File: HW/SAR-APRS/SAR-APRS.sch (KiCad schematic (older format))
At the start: 0 parts

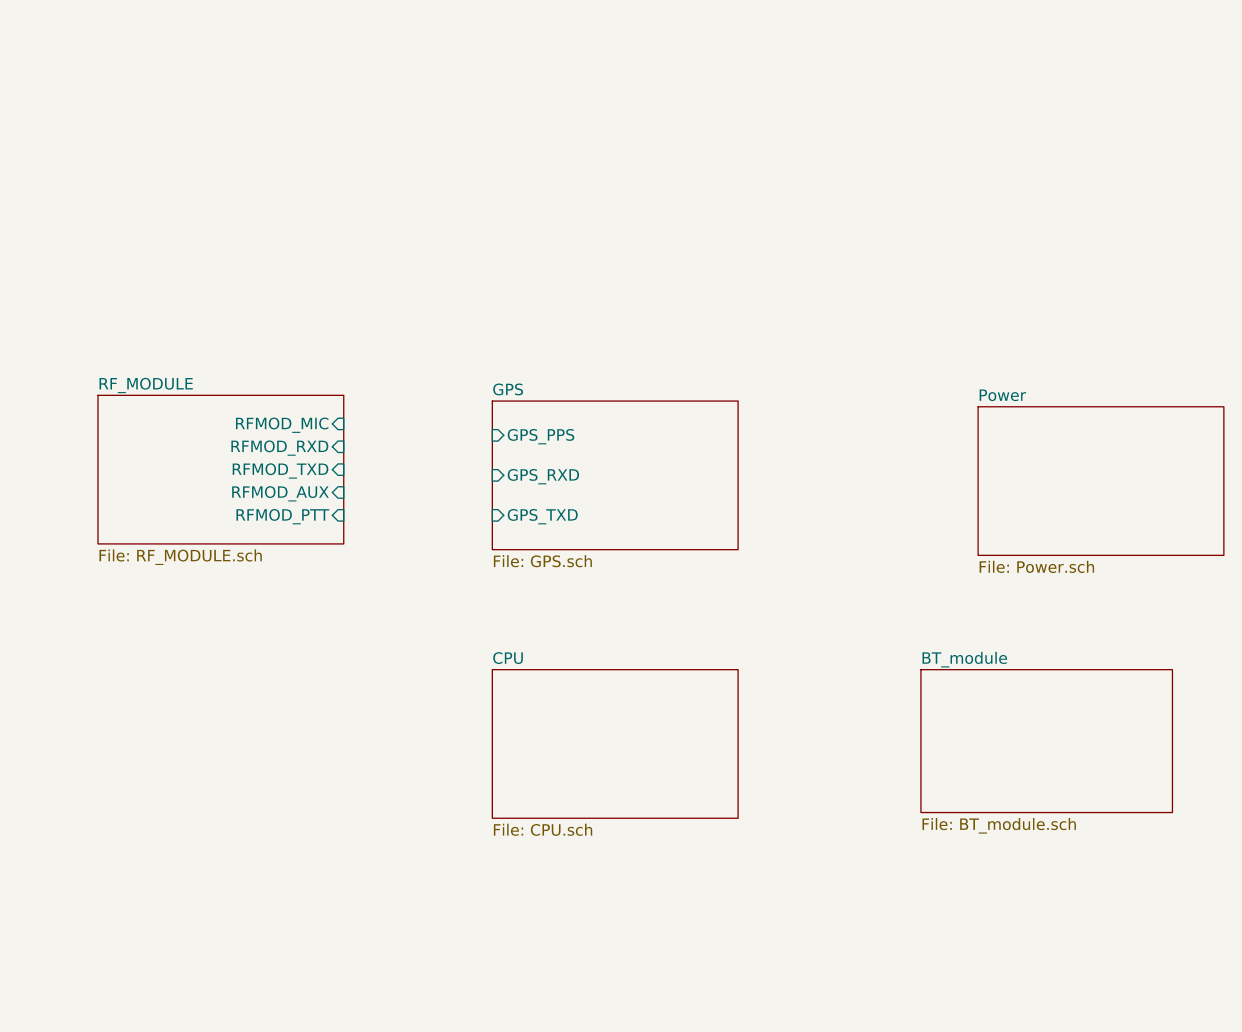
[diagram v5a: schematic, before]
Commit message: schematic update
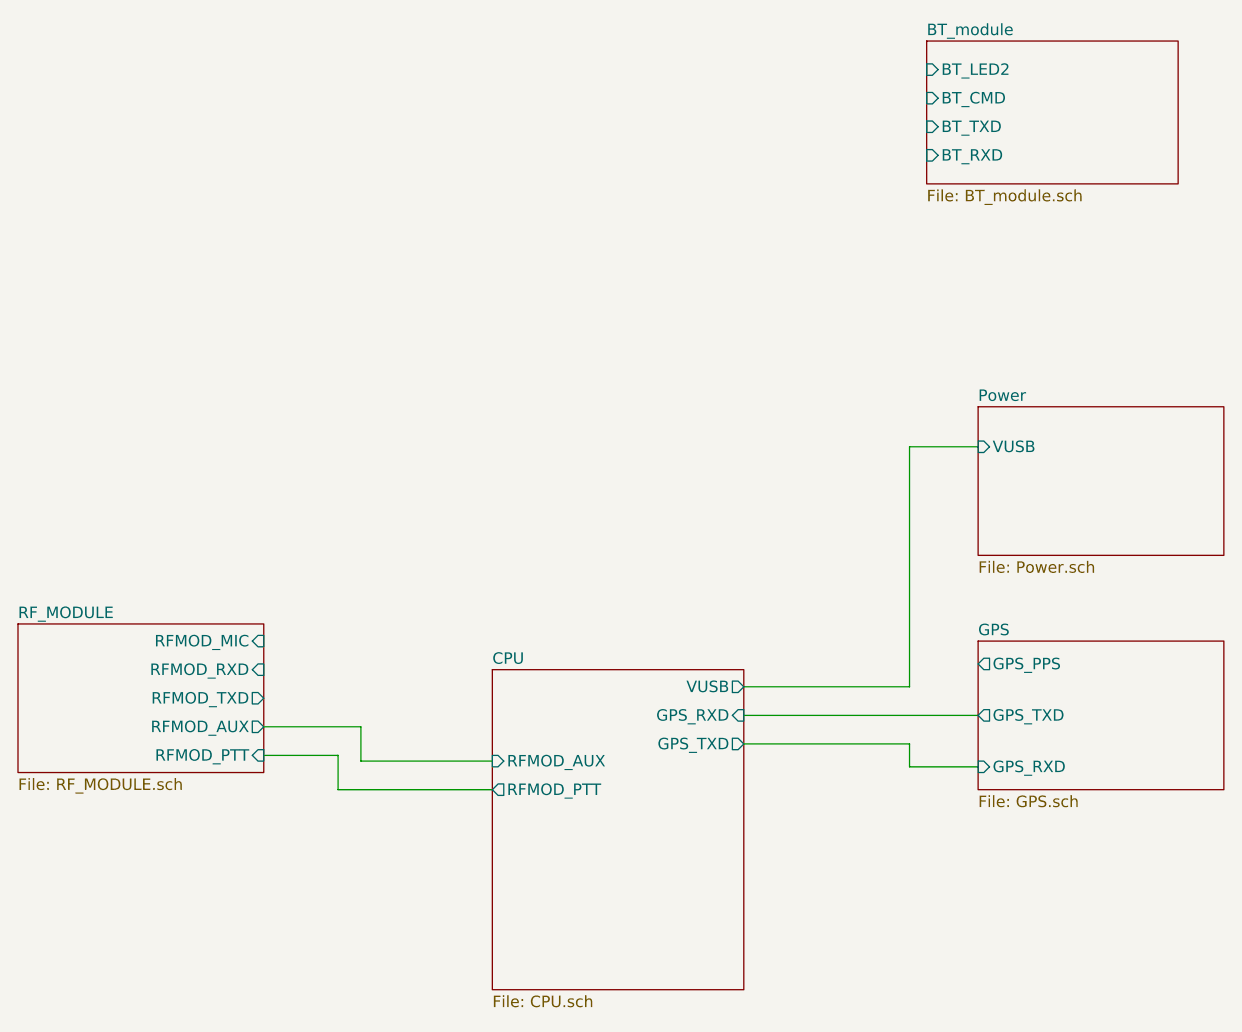
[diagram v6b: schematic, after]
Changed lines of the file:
@@
 $EndDescr
 $Sheet
-S 5700 4775 1075 650
+S 5350 5775 1075 650
 U 5C8B81A5
 F0 "RF_MODULE" 50
 F1 "RF_MODULE.sch" 50
-F2 "RFMOD_MIC" I R 6775 4900 50
-F3 "RFMOD_RXD" I R 6775 5000 50
-F4 "RFMOD_TXD" I R 6775 5100 50
-F5 "RFMOD_AUX" I R 6775 5200 50
-F6 "RFMOD_PTT" I R 6775 5300 50
+F2 "RFMOD_MIC" I R 6425 5850 50
+F3 "RFMOD_RXD" I R 6425 5975 50
+F4 "RFMOD_TXD" O R 6425 6100 50
+F5 "RFMOD_AUX" O R 6425 6225 50
+F6 "RFMOD_PTT" I R 6425 6350 50
 $EndSheet
 $Sheet
@@
 F0 "Power" 50
 F1 "Power.sch" 50
+F2 "VUSB" I L 9550 5000 50
 $EndSheet
 $Sheet
-S 7425 4800 1075 650
+S 7425 5975 1100 1400
+U 5CB07977
+F0 "CPU" 50
+F1 "CPU.sch" 50
+F2 "GPS_RXD" I R 8525 6175 50
+F3 "GPS_TXD" O R 8525 6300 50
+F4 "RFMOD_PTT" O L 7425 6500 50
+F5 "RFMOD_AUX" I L 7425 6375 50
+F6 "VUSB" O R 8525 6050 50
+$EndSheet
+$Sheet
+S 9325 3225 1100 625
+U 5C81D1BC
+F0 "BT_module" 50
+F1 "BT_module.sch" 50
+F2 "BT_LED2" I L 9325 3350 50
+F3 "BT_CMD" I L 9325 3475 50
+F4 "BT_TXD" I L 9325 3600 50
+F5 "BT_RXD" I L 9325 3725 50
+$EndSheet
+$Sheet
+S 9550 5850 1075 650
 U 5C97B601
 F0 "GPS" 50
 F1 "GPS.sch" 50
-F2 "GPS_PPS" I L 7425 4950 50
-F3 "GPS_RXD" I L 7425 5125 50
-F4 "GPS_TXD" I L 7425 5300 50
+F2 "GPS_PPS" O L 9550 5950 50
+F3 "GPS_TXD" O L 9550 6175 50
+F4 "GPS_RXD" I L 9550 6400 50
 $EndSheet
-$Sheet
-S 7425 5975 1075 650
-U 5CB07977
-F0 "CPU" 50
-F1 "CPU.sch" 50
-$EndSheet
-$Sheet
-S 9300 5975 1100 625
-U 5C81D1BC
-F0 "BT_module" 50
-F1 "BT_module.sch" 50
-$EndSheet
+Wire Wire Line
+	9550 6175 8525 6175
+Wire Wire Line
+	8525 6300 9250 6300
+Wire Wire Line
+	9250 6300 9250 6400
+Wire Wire Line
+	9250 6400 9550 6400
+Wire Wire Line
+	6425 6225 6850 6225
+Wire Wire Line
+	6850 6225 6850 6375
+Wire Wire Line
+	6850 6375 7425 6375
+Wire Wire Line
+	6425 6350 6750 6350
+Wire Wire Line
+	6750 6350 6750 6500
+Wire Wire Line
+	6750 6500 7425 6500
+Wire Wire Line
+	8525 6050 9250 6050
+Wire Wire Line
+	9250 6050 9250 5000
+Wire Wire Line
+	9250 5000 9550 5000
 $EndSCHEMATC

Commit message: schem and pcb update
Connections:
- wire segments 13 -> 14
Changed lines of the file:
@@
 EESchema Schematic File Version 4
 LIBS:SAR-APRS-cache
-EELAYER 28 0
+EELAYER 29 0
 EELAYER END
 $Descr A3 16535 11693
@@
 $EndDescr
 $Sheet
-S 5350 5775 1075 650
+S 5375 5000 1075 650
 U 5C8B81A5
 F0 "RF_MODULE" 50
 F1 "RF_MODULE.sch" 50
-F2 "RFMOD_MIC" I R 6425 5850 50
-F3 "RFMOD_RXD" I R 6425 5975 50
-F4 "RFMOD_TXD" O R 6425 6100 50
-F5 "RFMOD_AUX" O R 6425 6225 50
-F6 "RFMOD_PTT" I R 6425 6350 50
+F2 "RFMOD_MIC" I R 6450 5075 50
+F3 "RFMOD_RXD" I R 6450 5200 50
+F4 "RFMOD_TXD" O R 6450 5325 50
+F5 "RFMOD_AUX" O R 6450 5450 50
+F6 "RFMOD_PTT" I R 6450 5575 50
 $EndSheet
 $Sheet
-S 9550 4825 1075 650
+S 9650 3900 1075 650
 U 5C948828
 F0 "Power" 50
 F1 "Power.sch" 50
-F2 "VUSB" I L 9550 5000 50
+F2 "VUSB" I L 9650 4075 50
 $EndSheet
 $Sheet
-S 7425 5975 1100 1400
+S 7550 4950 1100 1625
 U 5CB07977
 F0 "CPU" 50
 F1 "CPU.sch" 50
-F2 "GPS_RXD" I R 8525 6175 50
-F3 "GPS_TXD" O R 8525 6300 50
-F4 "RFMOD_PTT" O L 7425 6500 50
-F5 "RFMOD_AUX" I L 7425 6375 50
-F6 "VUSB" O R 8525 6050 50
+F2 "GPS_RXD" I R 8650 5350 50
+F3 "GPS_TXD" O R 8650 5475 50
+F4 "RFMOD_PTT" O L 7550 5575 50
+F5 "RFMOD_AUX" I L 7550 5450 50
+F6 "VUSB" O R 8650 5025 50
+F7 "RFMOD_TXD" O L 7550 5200 50
+F8 "RFMOD_RXD" I L 7550 5325 50
+F9 "RFMOD_MIC" O L 7550 5075 50
+F10 "GPS_PPS" I R 8650 5200 50
+F11 "BT_TXD" O R 8650 6300 50
+F12 "BT_RXD" I R 8650 6425 50
+F13 "BT_LED2" O R 8650 6050 50
+F14 "BT_CMD" O R 8650 6175 50
 $EndSheet
 $Sheet
-S 9325 3225 1100 625
+S 9650 5925 1100 625
 U 5C81D1BC
 F0 "BT_module" 50
 F1 "BT_module.sch" 50
-F2 "BT_LED2" I L 9325 3350 50
-F3 "BT_CMD" I L 9325 3475 50
-F4 "BT_TXD" I L 9325 3600 50
-F5 "BT_RXD" I L 9325 3725 50
+F2 "BT_LED2" I L 9650 6050 50
+F3 "BT_CMD" I L 9650 6175 50
+F4 "BT_TXD" I L 9650 6300 50
+F5 "BT_RXD" I L 9650 6425 50
 $EndSheet
 $Sheet
-S 9550 5850 1075 650
+S 9650 4925 1075 650
 U 5C97B601
 F0 "GPS" 50
 F1 "GPS.sch" 50
-F2 "GPS_PPS" O L 9550 5950 50
-F3 "GPS_TXD" O L 9550 6175 50
-F4 "GPS_RXD" I L 9550 6400 50
+F2 "GPS_PPS" O L 9650 5200 50
+F3 "GPS_TXD" O L 9650 5350 50
+F4 "GPS_RXD" I L 9650 5475 50
 $EndSheet
 Wire Wire Line
-	9550 6175 8525 6175
+	9650 5350 8650 5350
 Wire Wire Line
-	8525 6300 9250 6300
+	8650 5025 9350 5025
 Wire Wire Line
-	9250 6300 9250 6400
+	9350 5025 9350 4075
 Wire Wire Line
-	9250 6400 9550 6400
+	9350 4075 9650 4075
 Wire Wire Line
-	6425 6225 6850 6225
+	6450 5575 7550 5575
 Wire Wire Line
-	6850 6225 6850 6375
+	6450 5450 7550 5450
 Wire Wire Line
-	6850 6375 7425 6375
+	6450 5325 7550 5325
 Wire Wire Line
-	6425 6350 6750 6350
+	6450 5200 7550 5200
 Wire Wire Line
-	6750 6350 6750 6500
+	7550 5075 6450 5075
 Wire Wire Line
-	6750 6500 7425 6500
+	8650 5475 9650 5475
 Wire Wire Line
-	8525 6050 9250 6050
+	8650 6425 9650 6425
 Wire Wire Line
-	9250 6050 9250 5000
+	8650 6300 9650 6300
 Wire Wire Line
-	9250 5000 9550 5000
+	8650 6175 9650 6175
+Wire Wire Line
+	8675 6050 9650 6050
 $EndSCHEMATC

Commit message: PCB update
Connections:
- wire segments 14 -> 15
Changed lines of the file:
@@
 F1 "RF_MODULE.sch" 50
 F2 "RFMOD_MIC" I R 6450 5075 50
-F3 "RFMOD_RXD" I R 6450 5200 50
-F4 "RFMOD_TXD" O R 6450 5325 50
+F3 "RFMOD_RXD" I R 6450 5325 50
+F4 "RFMOD_TXD" O R 6450 5200 50
 F5 "RFMOD_AUX" O R 6450 5450 50
 F6 "RFMOD_PTT" I R 6450 5575 50
@@
 	6450 5450 7550 5450
 Wire Wire Line
-	6450 5325 7550 5325
-Wire Wire Line
-	6450 5200 7550 5200
-Wire Wire Line
 	7550 5075 6450 5075
 Wire Wire Line
@@
 	8650 6175 9650 6175
 Wire Wire Line
-	8675 6050 9650 6050
+	9650 5200 8650 5200
+Wire Wire Line
+	8650 6050 9650 6050
+Wire Wire Line
+	6450 5200 7550 5200
+Wire Wire Line
+	6450 5325 7550 5325
 $EndSCHEMATC
